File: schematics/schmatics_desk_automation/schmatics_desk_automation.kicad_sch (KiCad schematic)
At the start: 14 parts, among them M1 Motor_DC, SW1 SW_Push_Dual, SW4 SW_Push_Dual, U1 L298N

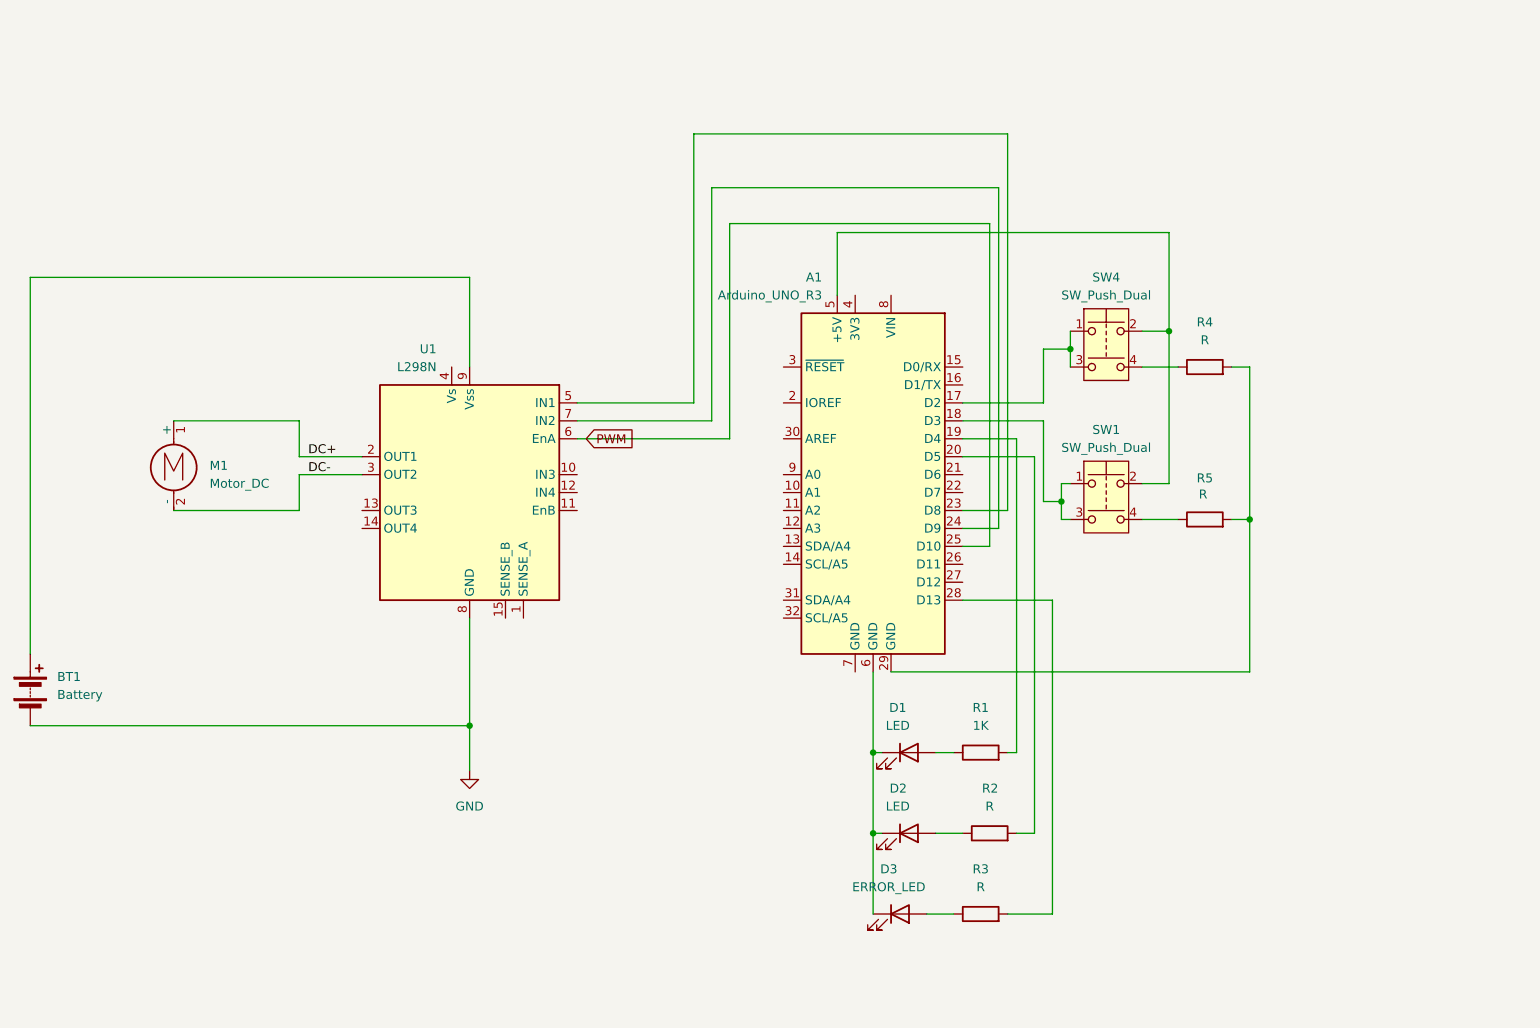
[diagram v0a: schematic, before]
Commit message: Add L298N interface library and enhance desk controller functionality
- Created a new symbol library for L298N interface in KiCad.
- Added autosave lock file for schematic design.
- Improved DeskController logic to handle error recovery from limit switches.
- Updated HAL initialization to set pin modes for upper and lower limit switches.
- Modified pin configuration for error LED and added definitions for limit switch inputs.
- Enhanced main loop to read limit switch states and integrate them into the application logic.
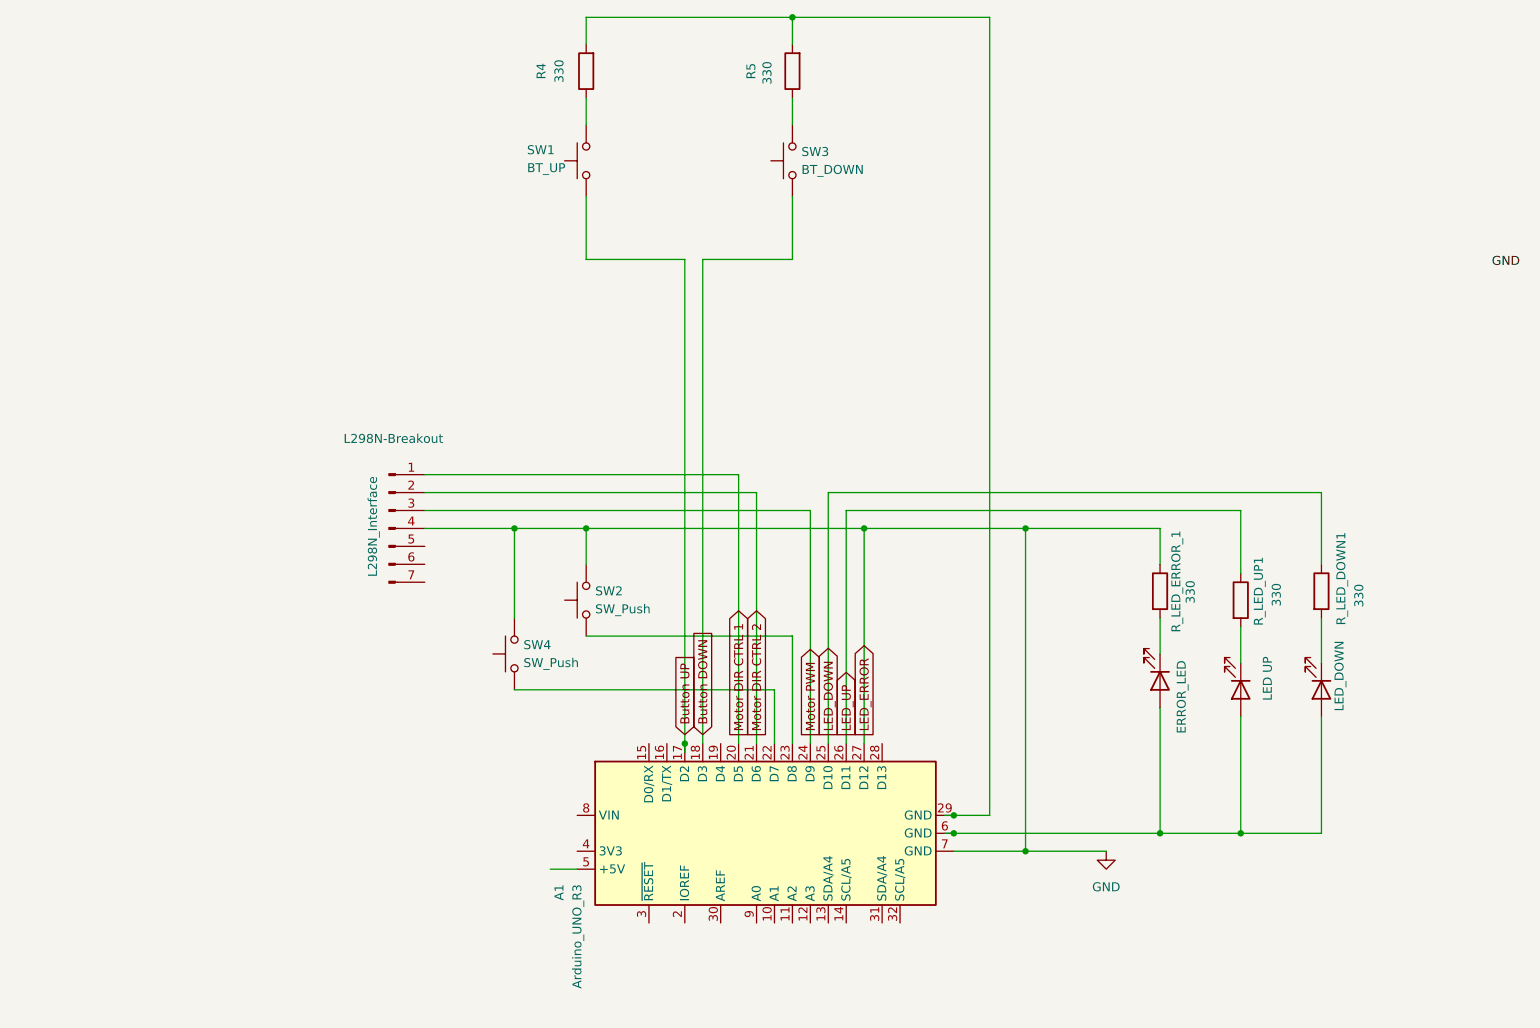
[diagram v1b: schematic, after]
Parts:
- removed BT1: Battery, DeskAutomation:S8211-46R, symbol Device:Battery
- removed M1: Motor_DC, symbol Motor:Motor_DC
- removed SW1, SW4: SW_Push_Dual, symbol Switch:SW_Push_Dual
- removed U1: L298N, Package_TO_SOT_THT:TO-220-15_P2.54x5.08mm_StaggerOdd_Lead4.58mm_Vertical, symbol Driver_Motor:L298N
- added L298N-Breakout: L298N_Interface, DeskAutomation:L298N Interface, symbol Connector:Conn_01x07_Pin
- added SW1: BT_UP, SW_PUSH_6mm_H5mm, symbol Switch:SW_Push
- added SW2, SW4: SW_Push, symbol Switch:SW_Push
- added SW3: BT_DOWN, SW_PUSH_6mm_H5mm, symbol Switch:SW_Push
- D1: value LED -> LED_DOWN; footprint (none) -> LED_THT:LED_D5.0mm
- D2: value LED -> LED UP; footprint (none) -> LED_THT:LED_D5.0mm
- D3: footprint (none) -> LED_THT:LED_D5.0mm
- R4, R5: value R -> 330; footprint (none) -> Resistor_THT:R_Axial_DIN0207_L6.3mm_D2.5mm_P2.54mm_Vertical
- R_LED_DOWN1: renamed from R1; value 1K -> 330; footprint (none) -> Resistor_THT:R_Axial_DIN0207_L6.3mm_D2.5mm_P2.54mm_Vertical
- R_LED_ERROR_1: renamed from R3; value R -> 330; footprint (none) -> Resistor_THT:R_Axial_DIN0207_L6.3mm_D2.5mm_P2.54mm_Vertical
- R_LED_UP1: renamed from R2; value R -> 330; footprint (none) -> Resistor_THT:R_Axial_DIN0207_L6.3mm_D2.5mm_P2.54mm_Vertical
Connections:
- net PWM is gone; now on net LED_DOWN: A1.25 (D10)
- net GND: now also A1.27 (D12), A1.7 (GND), R_LED_ERROR_1.1, L298N-Breakout.4 (Pin_4), SW2.2, SW4.2
- net Button DOWN: now reaches A1.18 (D3)
- net Button DOWN: now also SW3.1
- net at R5.1: now also SW3.2
- net at D2.2 (A): now also A1.6 (GND), D1.2 (A), D3.2 (A); no longer R_LED_UP1.1
- net at R_LED_UP1.2: now also D2.1 (K); no longer A1.20 (D5)
- net Button UP: now reaches A1.17 (D2)
- net Button UP: now also SW1.1
- net at R4.1: now also SW1.2
- net LED_DOWN: now reaches R_LED_DOWN1.1
- net LED_DOWN: no longer D1.2 (A)
- net at A1.23 (D8): now also SW2.1
- net Motor PWM: now reaches A1.24 (D9)
- net Motor PWM: now also L298N-Breakout.3 (Pin_3)
- net at R_LED_DOWN1.2: now also D1.1 (K); no longer A1.19 (D4)
- net at R_LED_ERROR_1.2: now also D3.1 (K); no longer A1.28 (D13)
- net Motor DIR CTRL 2: now reaches A1.21 (D6)
- net Motor DIR CTRL 2: now also L298N-Breakout.2 (Pin_2)
- net at A1.22 (D7): now also SW4.1
- net LED_UP: now reaches A1.26 (D11)
- net LED_UP: now also R_LED_UP1.1
- new net Motor DIR CTRL 1: A1.20 (D5), L298N-Breakout.1 (Pin_1)
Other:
- moved on the sheet: A1, R4, R5, R_LED_DOWN1, R_LED_ERROR_1, R_LED_UP1
